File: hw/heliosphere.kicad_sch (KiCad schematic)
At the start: 13 parts, among them J101 Conn_01x02

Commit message: footprint and schematic update
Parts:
- added J102: Conn_01x02, Connector_Wire:SolderWire-2.5sqmm_1x02_P8.8mm_D2.4mm_OD4.4mm, symbol Connector_Generic:Conn_01x02
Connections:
- net GND: now also J102.2 (Pin_2)
- net at J101.1 (Pin_1), R101.2: now also J102.1 (Pin_1)
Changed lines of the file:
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@@
   (junction (at 97.79 83.82) (diameter 0) (color 0 0 0 0)
   )
+  (junction (at 125.73 83.82) (diameter 0) (color 0 0 0 0)
+  )
   (junction (at 125.73 109.22) (diameter 0) (color 0 0 0 0)
   )
@@
   )
   (junction (at 59.69 83.82) (diameter 0) (color 0 0 0 0)
+  )
+  (junction (at 125.73 86.36) (diameter 0) (color 0 0 0 0)
   )
   (no_connect (at 63.5 87.63))
@@
     (stroke (width 0) (type default))
   )
+  (wire (pts (xy 125.73 83.82) (xy 139.7 83.82))
+    (stroke (width 0) (type default))
+  )
   (wire (pts (xy 50.8 109.22) (xy 63.5 109.22))
     (stroke (width 0) (type default))
@@
   )
   (wire (pts (xy 59.69 83.82) (xy 59.69 91.44))
+    (stroke (width 0) (type default))
+  )
+  (wire (pts (xy 125.73 86.36) (xy 139.7 86.36))
     (stroke (width 0) (type default))
   )
@@
         )
       )
+    )
+  )
+  (symbol (lib_id "Connector_Generic:Conn_01x02") (at 144.78 83.82 0) (unit 1)
+    (in_bom yes) (on_board yes) (dnp no)
+    (property "Reference" "J102" (at 138.43 78.74 0)
+      (effects (font (size 1.27 1.27)) (justify left))
+    )
+    (property "Value" "Conn_01x02" (at 138.43 81.28 0)
+      (effects (font (size 1.27 1.27)) (justify left))
+    )
+    (property "Footprint" "Connector_Wire:SolderWire-2.5sqmm_1x02_P8.8mm_D2.4mm_OD4.4mm" (at 144.78 83.82 0)
+      (effects (font (size 1.27 1.27)) hide)
+    )
+    (property "Datasheet" "~" (at 144.78 83.82 0)
+      (effects (font (size 1.27 1.27)) hide)
+    )
+    (pin "1")
+    (pin "2")
+    (instances
+      (project "heliosphere"
+        (path "/d40c06f6-44f1-4ac1-bb0a-5c24da31519b"
+          (reference "J102") (unit 1)
+        )
+      )

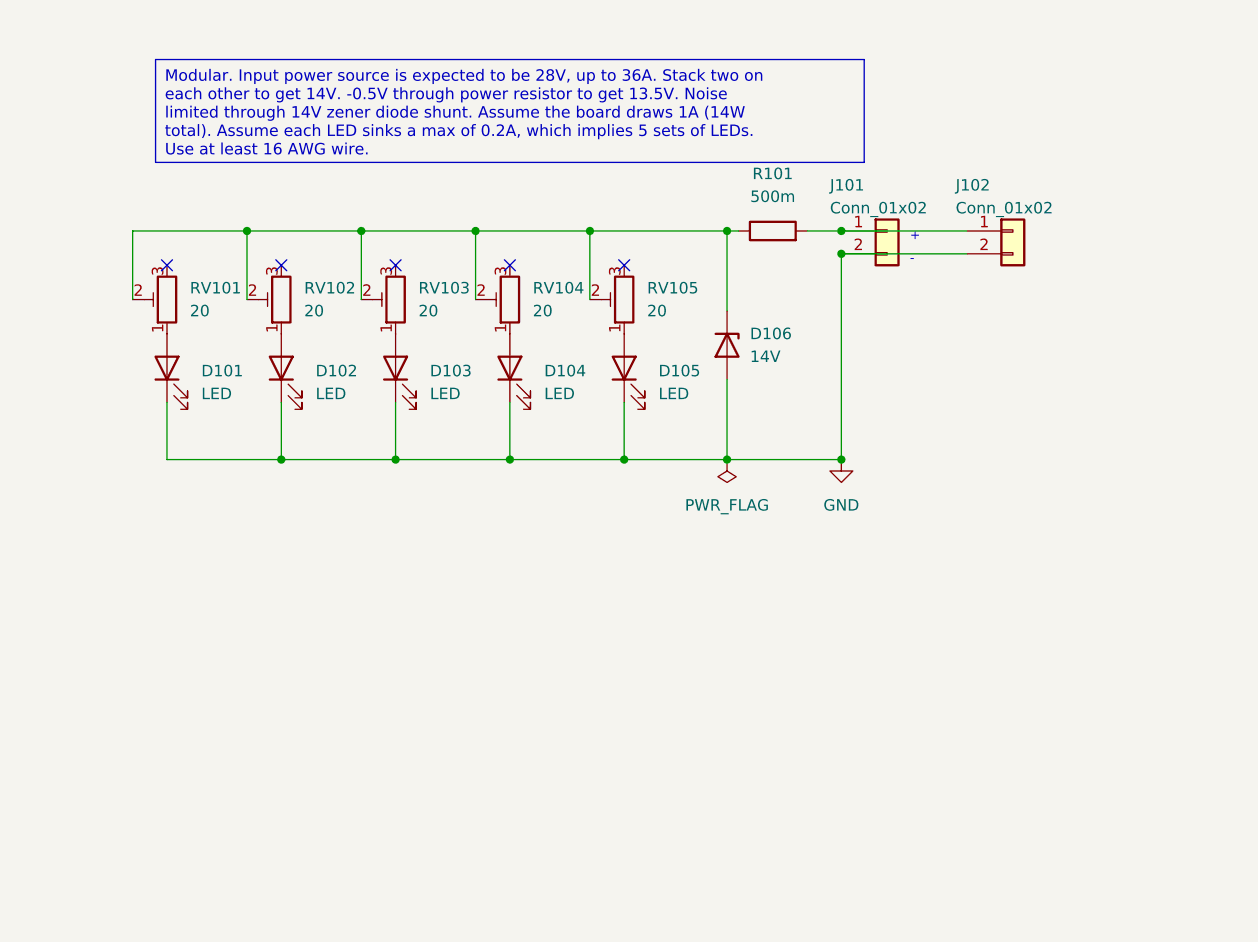
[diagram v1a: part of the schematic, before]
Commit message: swap trimpot for available one on mouser
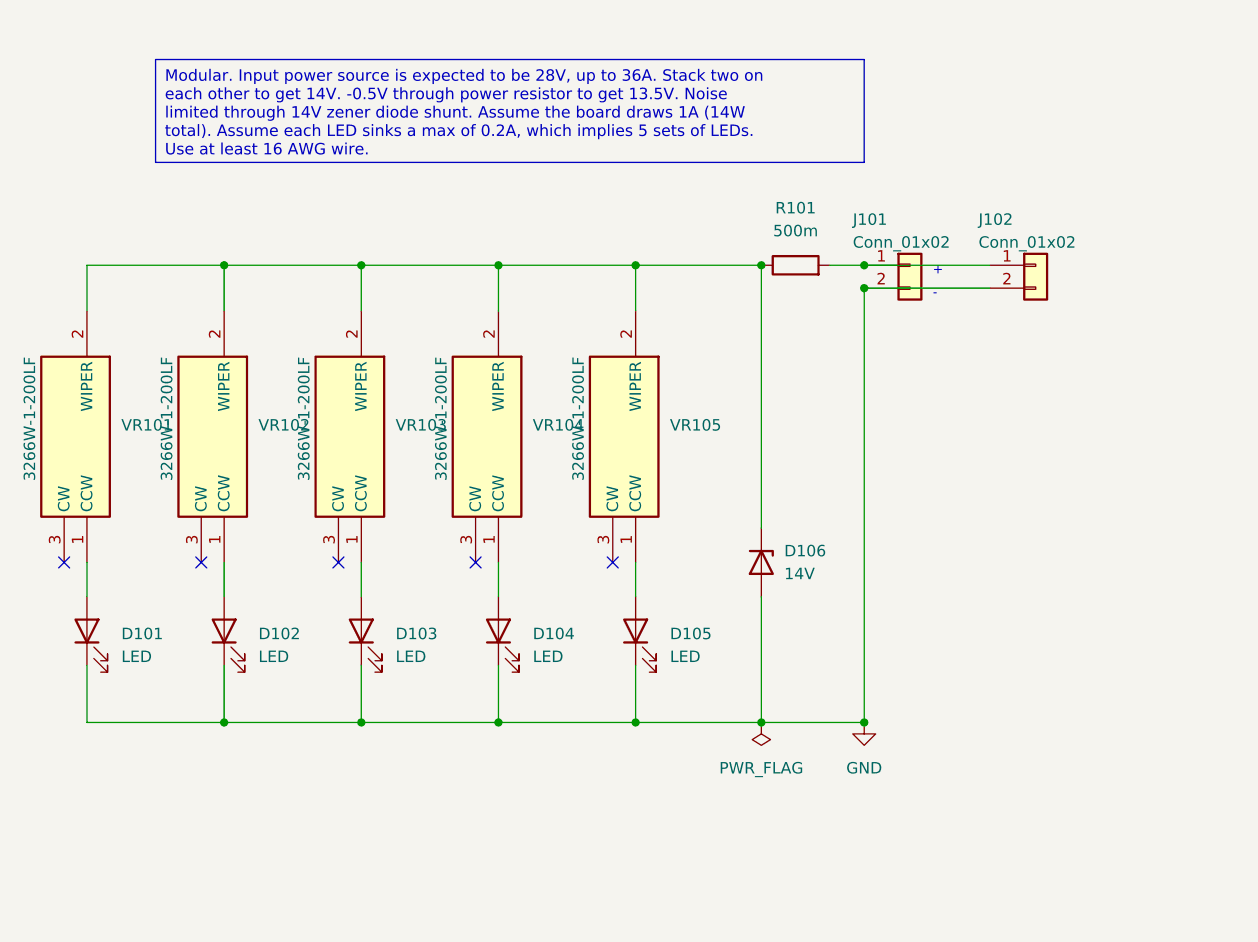
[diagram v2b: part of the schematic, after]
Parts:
- removed RV101, RV102, RV103, RV104, RV105: 20, footprints:dale_1680_trimpot, symbol Device:R_Potentiometer_Trim
- added VR101, VR102, VR103, VR104, VR105: 3266W-1-200LF, footprints:bourns3266W_1_200LF, symbol bourns_3266W_1_200LF:3266W-1-200LF
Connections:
- net at D102.2 (A): now also VR102.1 (CCW)
- net at D103.2 (A): now also VR103.1 (CCW)
- net at D106.1 (K), R101.1: now also VR101.2 (WIPER), VR102.2 (WIPER), VR103.2 (WIPER), VR104.2 (WIPER), VR105.2 (WIPER)
- net at D105.2 (A): now also VR105.1 (CCW)
- net at D104.2 (A): now also VR104.1 (CCW)
- net at D101.2 (A): now also VR101.1 (CCW)
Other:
- moved on the sheet: D101, D102, D103, D104, D105, D106, J101, J102, R101
